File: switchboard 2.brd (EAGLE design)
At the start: 100 x 60 mm, 203 parts, among them IC1 MT8816AP, IC10 Z8F2480SO, IC11 LMV321M5, IC12 74HC595D, IC14 74LVC1G125DBV, IC15 74LVC1G125DBV, IC16 LM2940, IC17 PC817S OPTO, IC2 NE5532D, IC3 TC7660-SOIC, IC4 TC7660-SOIC, IC5 FT232RL, IC6 78L05F, IC7 LD117AS33TR, IC8 SPI_MEMORY-SOIC, IC9 NE5532D, Q1 2N7002, Q2 2N7002, X1 MINI-USB-SCHIELD-32005-301

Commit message: Polarity protection changed from series diode to PMOS. Pinheaders addded to access the MCU pins directly. V+ and Vcc power supply symbols changed to +9V and +5V_AN, respectively. Spark gaps added.
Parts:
- removed U$5, U$6, U$7, U$8: SPARK_GAP, PATSKO:SPARK-GAP-8
- added GAP1, GAP2, GAP3, GAP4, GAP5, GAP6: SPARK_GAP, PATSKO:SPARK-GAP-8
- added P_EXTRA: (no value), pinhead:1X05
- added P_I2C: (no value), pinhead:1X03
- added P_SPI: (no value), pinhead:1X04
- added Q3: BSS84, transistor-small-signal:SOT23
- IC16: value LM2940 -> LM2940-9
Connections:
- net V+ renamed +5V_AN
- removed net C_SW3: IC1.25, IC10.15, R10.2
- removed net C_SW4: IC1.4, IC10.18, R11.2
- removed net VCC: C22.1, C26.1, C27.1, C30.1, C9.+, D5.A, D6.C, IC16.3, IC4.8, IC6.3, IC7.3, JP12.1, JP12.2, JP13.1, JP13.2, JP14.1, JP14.2, SJ6.2
- new net +9V: C22.1, C26.1, C27.1, C30.1, C9.+, D5.A, D6.A, IC16.3, IC4.8, IC6.3, IC7.3, JP12.1, JP12.2, JP13.1, JP13.2, JP14.1, JP14.2, SJ6.2
- new net C_SW3/SCL: IC1.25, IC10.15, P_I2C.2, R10.2
- new net C_SW4/SDA: IC1.4, IC10.18, P_I2C.1, R11.2
- new net N$48: GAP6.P$1, P_POWER_IN.2, Q3.3
- net CS_MEM: now also P_EXTRA.2
- net CS_SHIFT: now also P_EXTRA.1
- net C_SW5: now also P_EXTRA.3
- net C_SW6: now also P_EXTRA.5
- net C_SW7: now also P_EXTRA.4
- net GND: now also GAP1.P$2, GAP2.P$2, GAP3.P$2, GAP4.P$2, GAP5.P$2, GAP6.P$2, P_I2C.3, P_SPI.4, Q3.1; no longer U$5.P$2, U$6.P$2, U$7.P$2, U$8.P$2
- net INPUT1: now also GAP2.P$1; no longer U$5.P$1
- net INPUT2: now also GAP4.P$1; no longer U$6.P$1
- net MISO: now also P_SPI.1
- net MOSI: now also P_SPI.2
- net N$25: now also D6.C, Q3.2; no longer D6.A, P_POWER_IN.2
- net N$34: now also GAP1.P$1
- net OUTPUT1: now also GAP3.P$1; no longer U$7.P$1
- net OUTPUT2: now also GAP5.P$1; no longer U$8.P$1
- net SCK: now also P_SPI.3
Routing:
- net VCC: track 12.3 -> 0.00 mm
- net +9V: track 0.00 -> 9.64 mm

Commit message: Signal names changed to clarify the direction to and from external effects.
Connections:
- net EIN_1 renamed FROM_EFF_1
- net EIN_10 renamed FROM_EFF_10
- net EIN_11 renamed FROM_EFF_11
- net EIN_2 renamed FROM_EFF_2
- net EIN_3 renamed FROM_EFF_3
- net EIN_4 renamed FROM_EFF_4
- net EIN_5 renamed FROM_EFF_5
- net EIN_6 renamed FROM_EFF_6
- net EIN_7 renamed FROM_EFF_7
- net EIN_8 renamed FROM_EFF_8
- net EIN_9 renamed FROM_EFF_9
- net EOUT_1 renamed TO_EFF_1
- net EOUT_2 renamed TO_EFF_2
- net EOUT_3 renamed TO_EFF_3
- net EOUT_4 renamed TO_EFF_4
- net EOUT_5 renamed TO_EFF_5
- net EOUT_6 renamed TO_EFF_6
- net SWIN_2 renamed SW_IN_2
- net SWOUT_2-EOUT_7 renamed SWOUT_2-TO_EFF_7
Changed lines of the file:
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@@
 <wire x1="27.305" y1="77.47" x2="29.845" y2="77.47" width="0" layer="19" extent="1-1"/>
 </signal>
-<signal name="EOUT_1">
+<signal name="TO_EFF_1">
 <contactref element="IC1" pad="41"/>
 <contactref element="C41" pad="1"/>
@@
 <wire x1="67.31" y1="20.8" x2="-253.58" y2="-641.985" width="0" layer="19" extent="1-1"/>
 </signal>
-<signal name="EOUT_2">
+<signal name="TO_EFF_2">
 <contactref element="IC1" pad="43"/>
 <contactref element="C42" pad="1"/>
@@
 <wire x1="64.77" y1="20.8" x2="-249.135" y2="-641.985" width="0" layer="19" extent="1-1"/>
 </signal>
-<signal name="EOUT_3">
+<signal name="TO_EFF_3">
 <contactref element="IC1" pad="1"/>
 <contactref element="C43" pad="1"/>
@@
 <wire x1="62.23" y1="20.8" x2="-244.69" y2="-641.985" width="0" layer="19" extent="1-1"/>
 </signal>
-<signal name="EOUT_4">
+<signal name="TO_EFF_4">
 <contactref element="IC1" pad="23"/>
 <contactref element="C44" pad="1"/>
@@
 <wire x1="62.23" y1="4.6" x2="-240.245" y2="-641.985" width="0" layer="19" extent="1-1"/>
 </signal>
-<signal name="EOUT_5">
+<signal name="TO_EFF_5">
 <contactref element="IC1" pad="21"/>
 <contactref element="C45" pad="1"/>
@@
 <wire x1="59.69" y1="4.6" x2="-253.58" y2="-647.065" width="0" layer="19" extent="1-1"/>
 </signal>
-<signal name="EOUT_6">
+<signal name="TO_EFF_6">
 <contactref element="IC1" pad="19"/>
 <contactref element="C46" pad="1"/>
@@
 <wire x1="-151.445" y1="-438.785" x2="-151.98" y2="-427.99" width="0" layer="19" extent="1-1"/>
 </signal>
-<signal name="SWOUT_2-EOUT_7">
+<signal name="SWOUT_2-TO_EFF_7">
 <contactref element="IC1" pad="17"/>
 <contactref element="IC2" pad="5"/>
@@
 <wire x1="83.185" y1="21.65" x2="54.13" y2="6.35" width="0" layer="19" extent="1-1"/>
 </signal>
-<signal name="EIN_2">
+<signal name="FROM_EFF_2">
 <contactref element="C36" pad="1"/>
 <contactref element="R30" pad="1"/>
@@
 <wire x1="-245.325" y1="-583.565" x2="-245.325" y2="-573.405" width="0" layer="19" extent="1-1"/>
 </signal>
-<signal name="EIN_3">
+<signal name="FROM_EFF_3">
 <contactref element="C37" pad="1"/>
 <contactref element="R31" pad="1"/>
@@
 <wire x1="-245.325" y1="-588.645" x2="-245.325" y2="-578.485" width="0" layer="19" extent="1-1"/>
 </signal>
-<signal name="EIN_4">
+<signal name="FROM_EFF_4">
 <contactref element="C38" pad="1"/>
 <contactref element="R36" pad="1"/>
@@
 <wire x1="70.33" y1="10.16" x2="-245.325" y2="-603.885" width="0" layer="19" extent="1-1"/>
 </signal>
-<signal name="EIN_5">
+<signal name="FROM_EFF_5">
 <contactref element="C39" pad="1"/>
 <contactref element="R37" pad="1"/>
@@
 <wire x1="54.13" y1="16.51" x2="-245.325" y2="-608.965" width="0" layer="19" extent="1-1"/>
 </signal>
-<signal name="EIN_6">
+<signal name="FROM_EFF_6">
 <contactref element="C40" pad="1"/>
 <contactref element="R38" pad="1"/>
@@
 <wire x1="76.835" y1="3.81" x2="-238.545" y2="-652.145" width="0" layer="19" extent="1-1"/>
 </signal>
-<signal name="SWIN_2">
+<signal name="SW_IN_2">
 <contactref element="IC2" pad="1"/>
 <contactref element="R18" pad="2"/>
@@
 <wire x1="79.375" y1="16.45" x2="70.33" y2="15.24" width="0" layer="19" extent="1-1"/>
 </signal>
-<signal name="EIN_1">
+<signal name="FROM_EFF_1">
 <contactref element="C35" pad="1"/>
 <contactref element="R1" pad="1"/>
@@
 <wire x1="45.085" y1="32.385" x2="-247.435" y2="-669.925" width="0" layer="19" extent="1-1"/>
 </signal>
-<signal name="EIN_7">
+<signal name="FROM_EFF_7">
 <contactref element="C47" pad="1"/>
 <contactref element="R32" pad="1"/>
@@
 <wire x1="54.13" y1="13.97" x2="-245.325" y2="-657.225" width="0" layer="19" extent="1-1"/>
 </signal>
-<signal name="EIN_8">
+<signal name="FROM_EFF_8">
 <contactref element="C48" pad="1"/>
 <contactref element="R33" pad="1"/>
@@
 <wire x1="54.13" y1="12.7" x2="-253.58" y2="-664.845" width="0" layer="19" extent="1-1"/>
 </signal>
-<signal name="EIN_9">
+<signal name="FROM_EFF_9">
 <contactref element="C49" pad="1"/>
 <contactref element="R50" pad="1"/>
@@
 <wire x1="53.975" y1="33.655" x2="-247.435" y2="-687.705" width="0" layer="19" extent="1-1"/>
 </signal>
-<signal name="EIN_10">
+<signal name="FROM_EFF_10">
 <contactref element="C50" pad="1"/>
 <contactref element="R51" pad="1"/>
@@
 <wire x1="54.13" y1="10.16" x2="-245.325" y2="-675.005" width="0" layer="19" extent="1-1"/>
 </signal>
-<signal name="EIN_11">
+<signal name="FROM_EFF_11">
 <contactref element="C51" pad="1"/>
 <contactref element="R52" pad="1"/>

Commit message: Pull-ups on crosspoint address lines and voltage translator on SCK/MOSI removed.
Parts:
- removed Q1, Q2: 2N7002, PATSKO:SOT23
- removed R10, R11, R12, R13, R59, R8, R9: 10k SMD, rcl:R0603
- removed R56, R57, R58: 10k, rcl:R0805
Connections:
- removed net MOSI_5V: IC1.42, Q2.3, R58.1
- removed net SCK_5V: IC1.20, Q1.3, R57.1
- net +3V3: no longer Q1.1, Q2.1
- net +5V: no longer R10.1, R11.1, R12.1, R13.1, R56.2, R57.2, R58.2, R59.1, R8.1, R9.1
- net BTN6/C_SW1: no longer R59.2
- net CS_SWITCH/AD0: no longer R56.1
- net C_SW2: no longer R8.2
- net C_SW3/SCL: no longer R10.2
- net C_SW4/SDA: no longer R11.2
- net C_SW5: no longer R12.2
- net C_SW6: no longer R13.2
- net C_SW7: no longer R9.2
- net MOSI: now also IC1.42; no longer Q2.2
- net SCK: now also IC1.20; no longer Q1.2

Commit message: Thru-hole pinheaders changed to SMD pinheaders.
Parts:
- removed H4: MOUNT-PAD-ROUND2.8, holes:2,8-PAD
- removed JP12, JP13, JP14, JP16, JP17, JP19, JP20: (no value), pinhead:2X03
- removed JP21, JP22, JP23, JP4, JP5, JP6, JP7, JP8, JP9: (no value), pinhead:1X02
- added JP26, JP27, JP28: (no value), pinhead-2:2X06SMD
- JP1, JP2, JP3: device pinhead:1X02 -> pinhead-2:2X03SMD
- JP10, JP15: device pinhead:2X03 -> pinhead-2:2X06SMD
- moved H3 44.9 mm to (50.0, 5.00)
- moved JP1 30.4 mm to (41.3, 6.35)
- moved JP10 22.3 mm to (66.7, 22.2), turned to 0 degrees
- moved JP15 21.6 mm to (67.3, 8.26), turned to 0 degrees
- moved JP2 17.3 mm to (31.1, 6.35)
- moved IC1 10.1 mm to (65.7, 22.2), flipped to the bottom, turned to 90 degrees
- moved JP3 4.58 mm to (21.0, 6.35)
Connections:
- removed net N$65: C50.2, JP20.6
- removed net N$66: C51.2, JP20.4
- removed net N$67: C52.2, JP20.2
- new net N$49: C48.2, JP28.3
- new net N$50: C49.2, JP28.5
- new net N$51: C50.2, JP28.7
- net +18V: now also JP1.5, JP1.6, JP2.5, JP2.6, JP3.5, JP3.6; no longer JP12.5, JP12.6, JP13.5, JP13.6, JP14.5, JP14.6
- net +9V: now also JP1.1, JP1.2, JP2.1, JP2.2, JP3.1, JP3.2; no longer JP12.1, JP12.2, JP13.1, JP13.2, JP14.1, JP14.2
- net BTN0: now also JP10.1, JP10.7, JP15.1, JP15.7; no longer JP23.1, JP3.1, JP6.1, JP9.1
- net BTN1: now also JP10.3, JP10.9, JP15.3, JP15.9; no longer JP2.1, JP22.1, JP5.1, JP8.1
- net BTN2: now also JP10.11, JP10.5, JP15.11, JP15.5; no longer JP1.1, JP21.1, JP4.1, JP7.1
- net BTN3: now also JP10.2, JP10.4, JP10.6; no longer JP1.2, JP2.2, JP3.2
- net BTN4: now also JP10.10, JP10.12, JP10.8; no longer JP4.2, JP5.2, JP6.2
- net BTN5: now also JP15.2, JP15.4, JP15.6; no longer JP7.2, JP8.2, JP9.2
- net BTN6/C_SW1: now also JP15.10, JP15.12, JP15.8; no longer JP21.2, JP22.2, JP23.2
- net GND: now also JP1.3, JP1.4, JP2.3, JP2.4, JP26.10, JP26.12, JP26.2, JP26.4, JP26.6, JP26.8, JP27.10, JP27.12, JP27.2, JP27.4, JP27.6, JP27.8, JP28.10, JP28.12, JP28.2, JP28.4, JP28.6, JP28.8, JP3.3, JP3.4; no longer JP10.1, JP10.3, JP10.5, JP12.3, JP12.4, JP13.3, JP13.4, JP14.3, JP14.4, JP15.1, JP15.3, JP15.5, JP16.1, JP16.3, JP16.5, JP17.1, JP17.3, JP17.5, JP19.1, JP19.3, JP19.5, JP20.1, JP20.3, JP20.5
- net N$12: now also JP27.1; no longer JP10.6
- net N$15: now also JP27.3; no longer JP10.4
- net N$16: now also JP27.5; no longer JP10.2
- net N$17: now also JP27.7; no longer JP15.6
- net N$18: now also JP27.9; no longer JP15.4
- net N$19: now also JP27.11; no longer JP15.2
- net N$21: now also JP26.1; no longer JP16.6
- net N$32: now also JP26.3; no longer JP16.4
- net N$52: now also JP26.5; no longer JP16.2
- net N$53: now also JP26.7; no longer JP17.6
- net N$59: now also JP26.9; no longer JP17.4
- net N$62: now also JP26.11; no longer JP17.2
- net N$63: now also C51.2, JP28.9; no longer C48.2, JP19.4
- net N$64: now also C52.2, JP28.11; no longer C49.2, JP19.2
- net N$9: now also JP28.1; no longer JP19.6

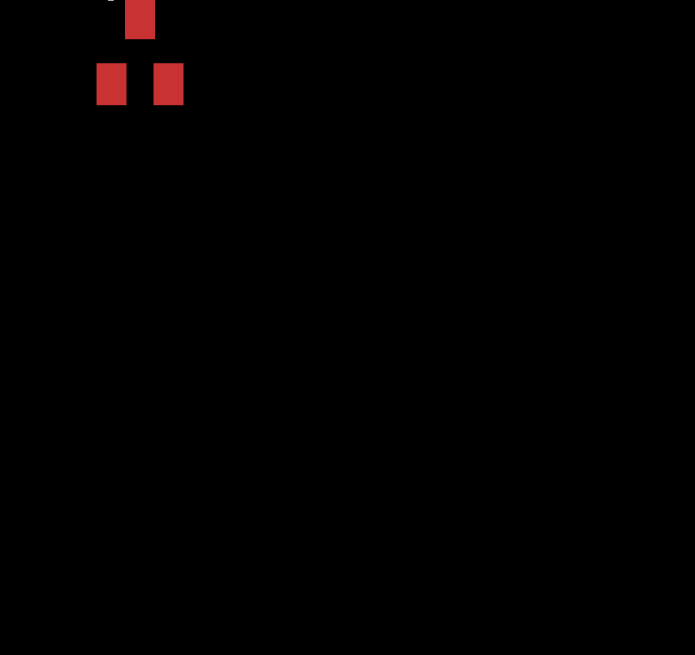
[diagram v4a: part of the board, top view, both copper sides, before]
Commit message: RC filter added to MIDI 3V3 supply. GND1 added to connect the MIDI In cable shield.
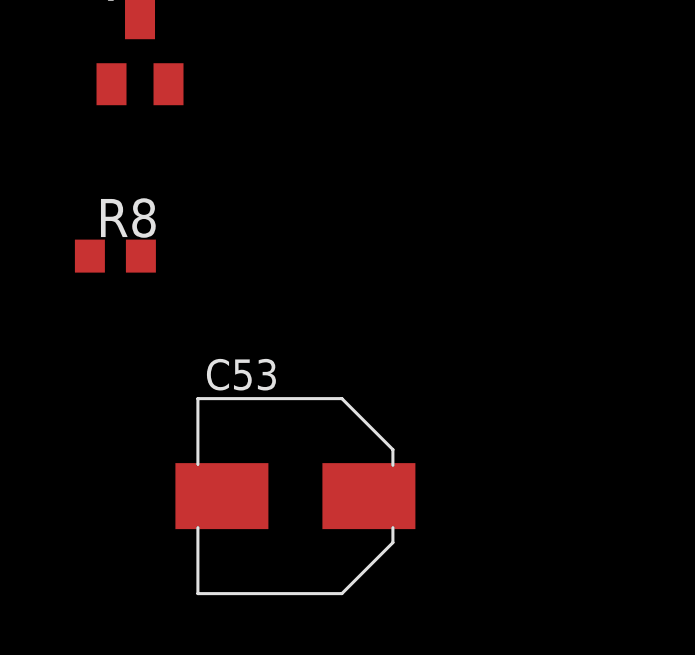
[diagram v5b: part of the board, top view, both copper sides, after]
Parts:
- added C53: 47u/25V, PATSKO:ALUMINUM-TANTALUM-CAP
- added R8: 100, rcl:R0603
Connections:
- new net 3V3_MIDI: C13.1, C18.1, C53.+, IC14.5, IC15.5, R35.1, R6.1, R8.1
- new net GND1: P_MIDI_IN.2
- net +3V3: now also R8.2; no longer C13.1, C18.1, IC14.5, IC15.5, R35.1, R6.1
- net GND: now also C53.-; no longer P_MIDI_IN.2

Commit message: Series resistors added to all audio effects inputs and outputs. Overvoltage protection added to audio and MIDI outputs. ESD protection added to MIDI inputs and outputs. USB_DETECT signal added to UART pinheader.
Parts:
- added D15, D16, D17, D18, D7, D8: LL4148, diode:MINIMELF
- added GAP10, GAP7, GAP8, GAP9: SPARK_GAP, PATSKO:SPARK-GAP-8
- added R10, R11, R12, R13, R56, R57, R58, R59, R72, R73, R74, R75, R76, R77, R78, R79, R80, R9: 100, rcl:R0603
- P_UART: device pinhead:1X03 -> pinhead:1X04
- Q3: value BSS84 -> FDN352AP
- moved P_UART 1044.0 mm to (-297.0, -981.0), turned to 0 degrees
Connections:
- new net N$65: C49.2, R59.2
- new net N$66: C50.2, R72.2
- new net N$67: C51.2, R73.2
- new net N$68: C52.2, R74.2
- new net N$69: JP27.3, R10.1
- new net N$70: JP27.9, R13.1
- new net N$71: JP27.7, R12.1
- new net N$72: JP27.5, R11.1
- new net N$73: JP28.3, R58.1
- new net N$74: JP28.9, R73.1
- new net N$75: JP28.5, R59.1
- new net N$76: JP28.7, R72.1
- net +5V_AN: now also D15.C, D7.C
- net 3V3_MIDI: now also D17.C
- net GND: now also D16.A, D18.A, D8.A, GAP7.P$2, GAP8.P$1, P_UART.4; no longer P_UART.1
- net GND1: now also GAP10.P$2, GAP9.P$1
- net MIDI_IN1: now also GAP9.P$2
- net MIDI_IN2: now also GAP10.P$1
- net MIDI_OUT1: now also GAP7.P$1
- net MIDI_OUT2: now also GAP8.P$2
- net N$12: now also R9.1; no longer C35.2
- net N$14: now also D7.A, D8.C
- net N$15: now also C35.2, R9.2; no longer C36.2, JP27.3
- net N$16: now also C36.2, R10.2; no longer C37.2, JP27.5
- net N$17: now also C37.2, R11.2; no longer C38.2, JP27.7
- net N$18: now also C38.2, R12.2; no longer C39.2, JP27.9
- net N$19: now also R56.1; no longer C40.2
- net N$2: now also D17.A, D18.C
- net N$21: now also R75.1; no longer C41.2
- net N$32: now also R76.1; no longer C42.2
- net N$49: now also C39.2, R13.2; no longer C48.2, JP28.3
- net N$50: now also C40.2, R56.2; no longer C49.2, JP28.5
- net N$51: now also C47.2, R57.2; no longer C50.2, JP28.7
- net N$52: now also R77.1; no longer C43.2
- net N$53: now also R78.1; no longer C44.2
- net N$56: now also D15.A, D16.C
- net N$59: now also R79.1; no longer C45.2
- net N$62: now also R80.1; no longer C46.2
- net N$63: now also C48.2, R58.2; no longer C51.2, JP28.9
- net N$64: now also R74.1; no longer C52.2
- net N$9: now also R57.1; no longer C47.2
- net UART_RX: now also P_UART.3; no longer P_UART.2
- net UART_TX: now also P_UART.2; no longer P_UART.3
- net USB_DETECT: now also P_UART.1

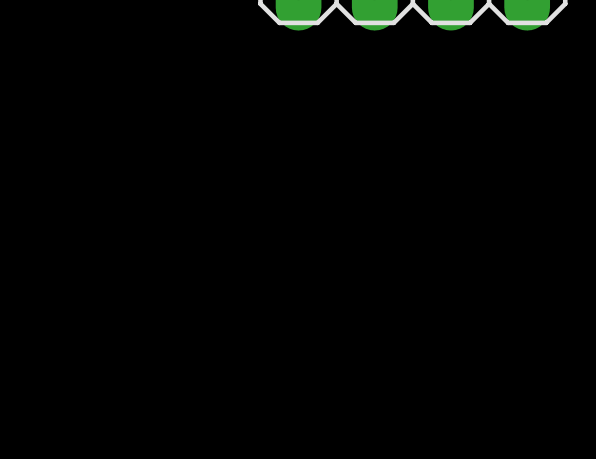
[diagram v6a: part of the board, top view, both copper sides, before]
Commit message: ESD protection with TPD2E001 added to USB inputs.
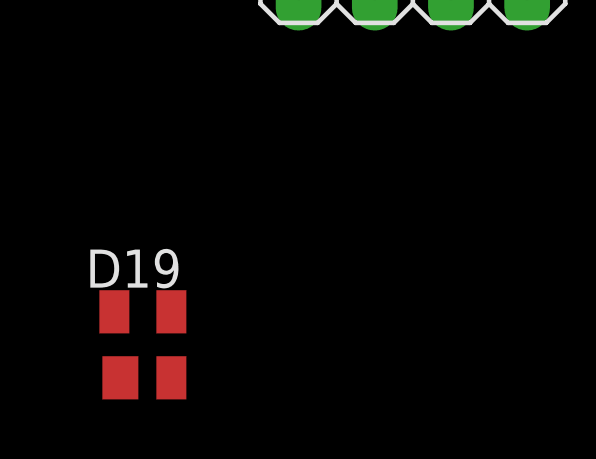
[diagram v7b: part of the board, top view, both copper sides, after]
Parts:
- added D19: (no value), PATSKO:SOT143B
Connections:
- net D+: now also D19.2
- net D-: now also D19.3
- net GND: now also D19.1
- net VIN_USB: now also D19.4
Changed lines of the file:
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@@
 <element name="GAP10" library="PATSKO" package="SPARK-GAP-8" value="SPARK_GAP" x="-308" y="-971"/>
 <element name="P_UART" library="pinhead" package="1X04" value="" x="-297" y="-981"/>
+<element name="D19" library="PATSKO" package="SOT143B" value="" x="-306" y="-993"/>
 </elements>
 <signals>
@@
 <contactref element="GAP8" pad="P$1"/>
 <contactref element="P_UART" pad="4"/>
+<contactref element="D19" pad="1"/>
 <wire x1="-220.56" y1="-529.59" x2="-236.13" y2="-526.415" width="0" layer="19" extent="1-1"/>
 <wire x1="-218.86" y1="-524.51" x2="-220.56" y2="-529.59" width="0" layer="19" extent="1-1"/>
@@
 <wire x1="-301.492" y1="-971" x2="-295.3" y2="-966" width="0" layer="19" extent="1-1"/>
 <wire x1="-293.19" y1="-981" x2="-289.508" y2="-971" width="0" layer="19" extent="1-1"/>
+<wire x1="-306.75" y1="-994.1" x2="-293.19" y2="-981" width="0" layer="19" extent="1-1"/>
 <wire x1="-47.945" y1="-48.895" x2="-71.54" y2="-280.035" width="0" layer="19" extent="1-1"/>
 <wire x1="-40.425" y1="-43.18" x2="-47.945" y2="-48.895" width="0" layer="19" extent="1-1"/>
@@
 <contactref element="IC5" pad="16"/>
 <contactref element="JP11" pad="4"/>
+<contactref element="D19" pad="3"/>
 <wire x1="11.43" y1="31.75" x2="4.63" y2="40.24" width="0" layer="19" extent="16-16"/>
 <wire x1="7.445" y1="28.41" x2="11.43" y2="31.75" width="0" layer="19" extent="16-16"/>
+<wire x1="-305.05" y1="-991.9" x2="4.63" y2="40.24" width="0" layer="19" extent="1-16"/>
 </signal>
 <signal name="D+">
@@
 <contactref element="IC5" pad="15"/>
 <contactref element="JP11" pad="3"/>
+<contactref element="D19" pad="2"/>
 <wire x1="7.445" y1="29.21" x2="4.63" y2="39.59" width="0" layer="19" extent="16-16"/>
 <wire x1="11.43" y1="29.21" x2="7.445" y2="29.21" width="0" layer="19" extent="16-16"/>
+<wire x1="-305.05" y1="-994.1" x2="4.63" y2="39.59" width="0" layer="19" extent="1-16"/>
 </signal>
 <signal name="5V_USB">
@@
 <contactref element="L1" pad="1"/>
 <contactref element="JP11" pad="5"/>
+<contactref element="D19" pad="4"/>
+<wire x1="-306.95" y1="-991.9" x2="-151.445" y2="-488.95" width="0" layer="19" extent="1-1"/>
 <wire x1="7.445" y1="27.61" x2="-151.445" y2="-488.95" width="0" layer="19" extent="1-16"/>
 <wire x1="11.43" y1="34.29" x2="7.445" y2="27.61" width="0" layer="19" extent="16-16"/>
